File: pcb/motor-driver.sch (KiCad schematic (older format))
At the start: 0 parts

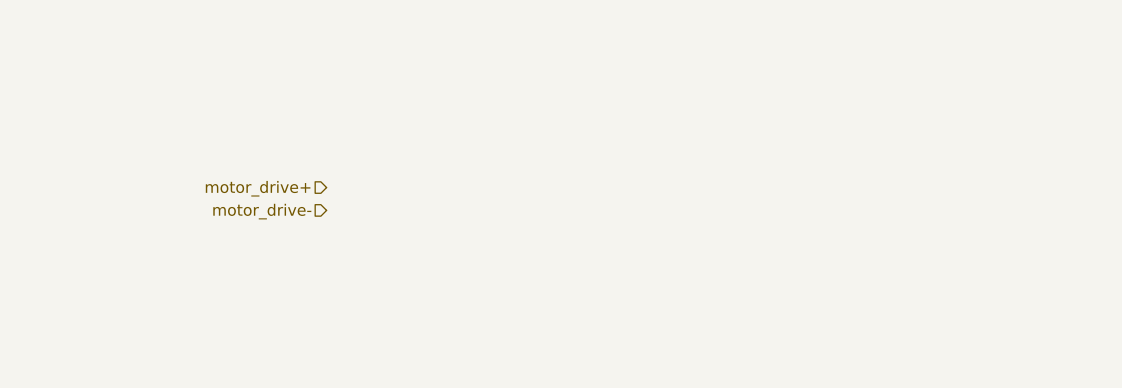
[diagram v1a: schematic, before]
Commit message: added motor driver schematic
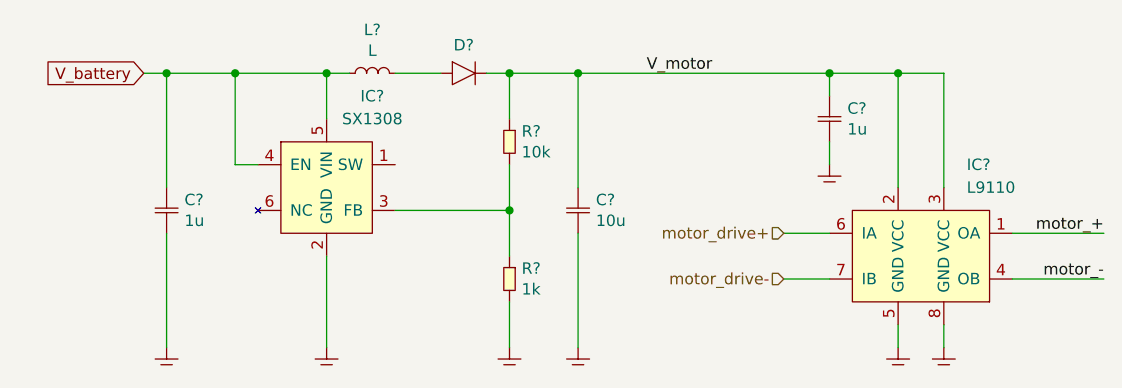
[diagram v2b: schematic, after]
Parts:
- added C? (x2): 1u, SMT:0603, symbol generic:C
- added C?: 10u, SMT:0603, symbol generic:C
- added D?: D, SMT:0603, symbol generic:D
- added GND? (x7): GND, symbol generic:GND
- added IC?: L9110, symbol motor_drivers:L9110
- added IC?: SX1308, symbol Power:SX1308
- added L?: L, symbol generic:L
- added R?: 10k, SMT:0603, symbol generic:R
- added R?: 1k, SMT:0603, symbol generic:R
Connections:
- net motor_drive+: now also IC?.6 (IA)
- net motor_drive-: now also IC?.7 (IB)
- new net: IC?.3 (FB), R?.1, R?.2
- new net: D?.1 (A), L?.2
- new net GND: C?.2, C?.2, C?.2, GND?.~ (GND), GND?.~ (GND), GND?.~ (GND), GND?.~ (GND), GND?.~ (GND), GND?.~ (GND), GND?.~ (GND), IC?.2 (GND), IC?.5 (GND), IC?.8 (GND), R?.2
- new net V_battery: C?.1, IC?.4 (EN), IC?.5 (VIN), L?.1
- new net V_motor: C?.1, C?.1, D?.2 (K), IC?.2 (VCC), IC?.3 (VCC), R?.1
- new net motor_+: IC?.1 (OA)
- new net motor_-: IC?.4 (OB)
